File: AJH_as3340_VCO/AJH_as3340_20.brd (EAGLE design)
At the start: 27.9 x 110.5 mm, 99 parts, among them IC1 LM4040 5.0V, IC2 TL072D, IC3 TL072D, IC4 TL072D, IC5 CEM3340SOIC16, IC6 TL072D, IC7 TL072D

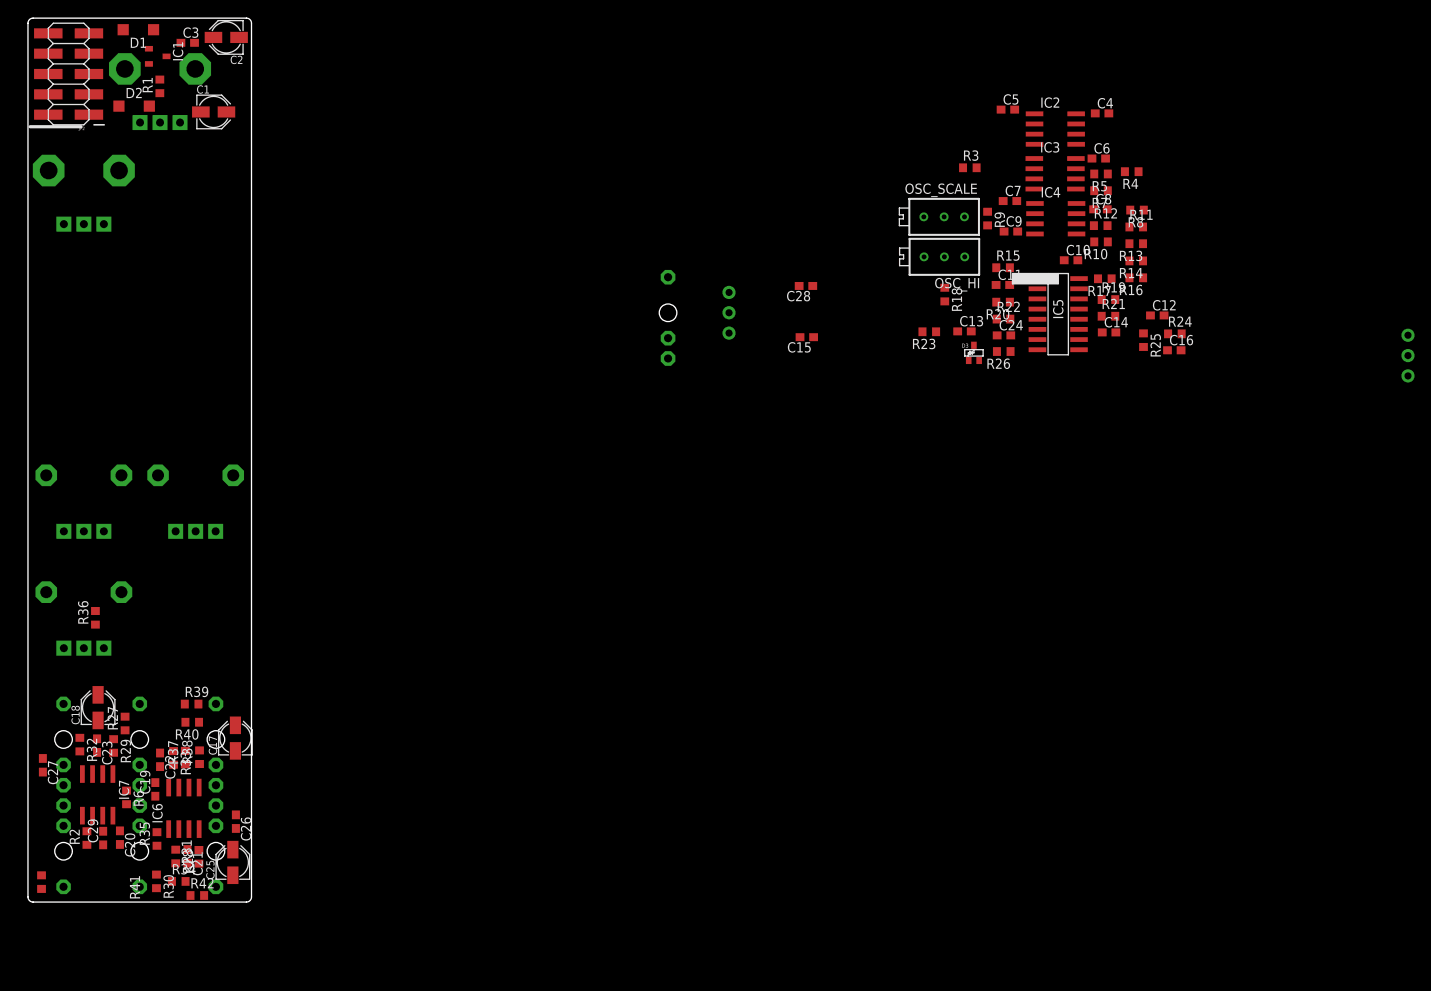
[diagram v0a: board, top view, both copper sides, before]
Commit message: Added Art Deco Panel template
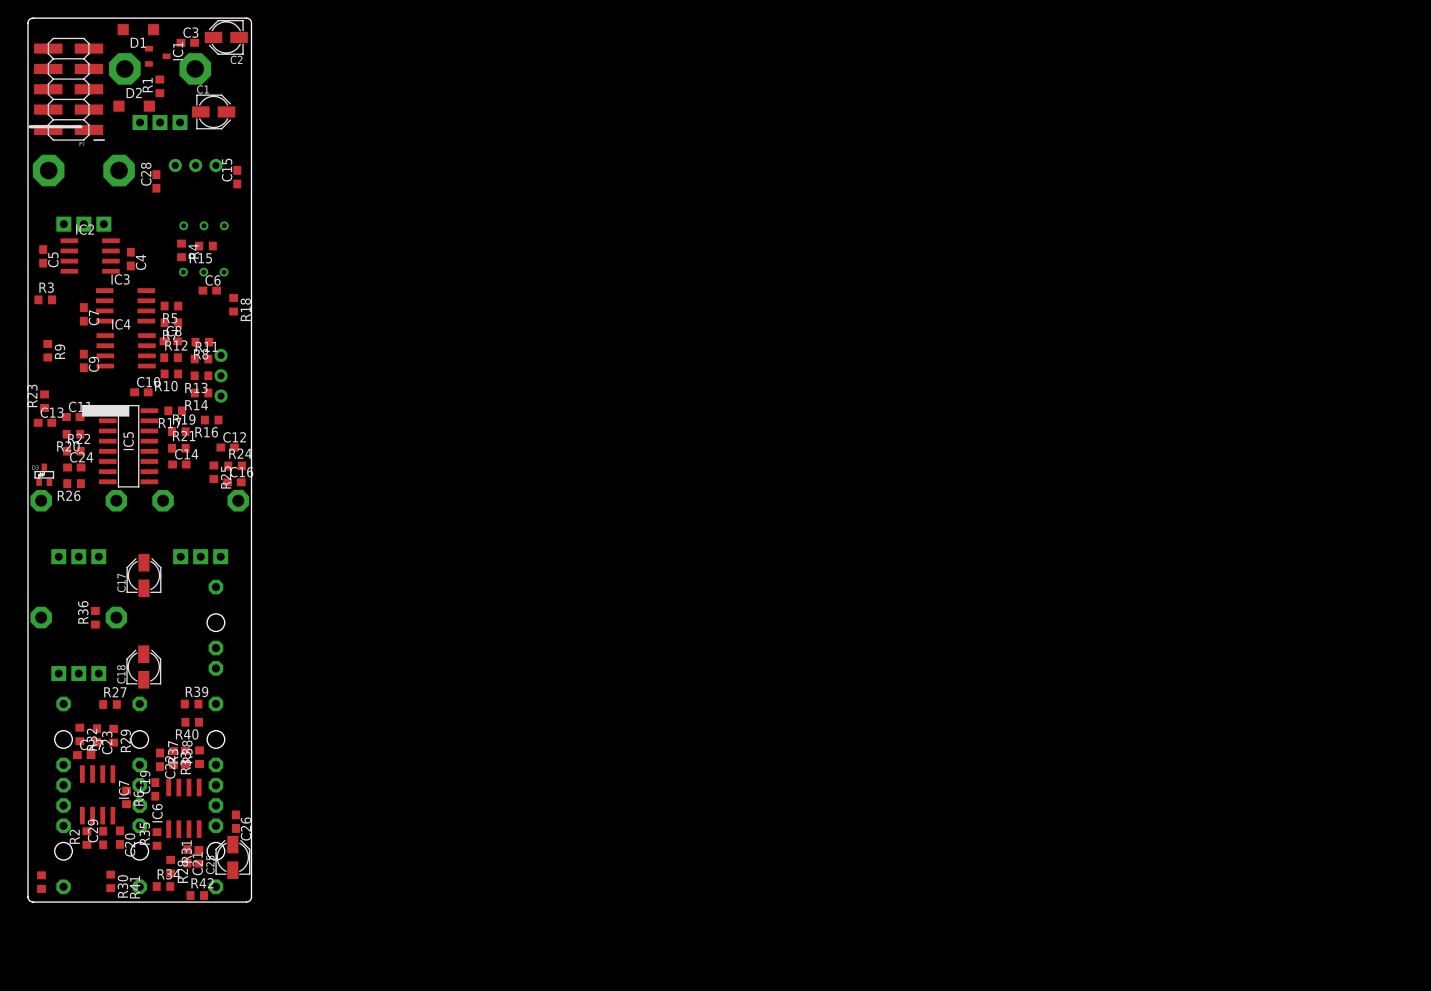
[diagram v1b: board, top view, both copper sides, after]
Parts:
- moved FM_SW 148.4 mm to (25.4, 74.7)
- moved C4 122.8 mm to (14.1, 89.3), turned to 270 degrees
- moved C5 122.0 mm to (3.17, 89.6), turned to 270 degrees
- moved IC2 121.7 mm to (9.04, 89.6)
- moved R4 119.2 mm to (20.5, 90.3), turned to 270 degrees
- moved R9 118.6 mm to (3.75, 77.8)
- moved C16 118.6 mm to (27.1, 61.4)
- moved R24 118.6 mm to (27.2, 63.4)
- moved R8 118.0 mm to (23.1, 78.9)
- moved R11 118.0 mm to (23.0, 76.8)
- moved R13 118.0 mm to (23.0, 74.7)
- moved R14 118.0 mm to (23.0, 72.5)
- moved C10 117.4 mm to (15.4, 72.6)
- moved C12 117.4 mm to (26.2, 65.7)
- moved C24 117.4 mm to (7.06, 63.2)
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
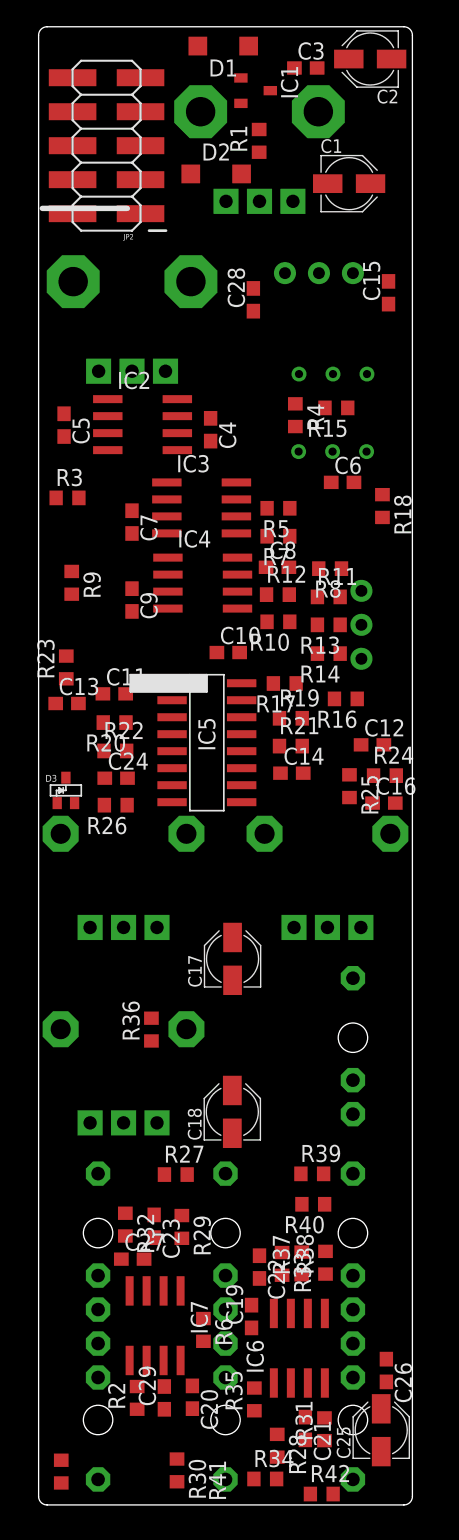
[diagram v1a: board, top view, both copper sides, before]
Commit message: Arranged parts to grid
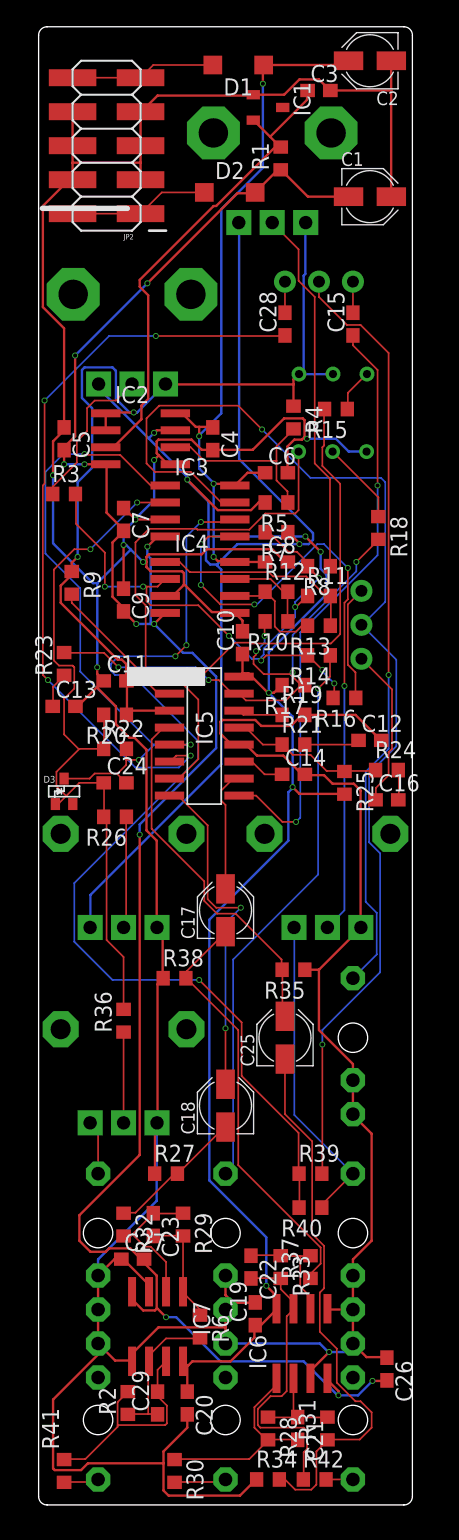
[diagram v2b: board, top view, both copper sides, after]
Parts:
- moved R35 32.2 mm to (20.3, 48.9), turned to 180 degrees
- moved C25 30.2 mm to (19.7, 43.8)
- moved R38 24.1 mm to (11.4, 48.3), turned to 0 degrees
- moved C6 4.99 mm to (19.1, 86.0)
- moved C17 3.67 mm to (15.2, 53.3)
- moved C15 3.55 mm to (24.8, 97.2)
- moved C28 2.98 mm to (19.7, 97.2)
- moved R36 2.19 mm to (7.62, 45.1)
- moved R1 2.08 mm to (19.4, 109.5)
- moved C3 1.95 mm to (22.2, 114.6)
- moved OSC_COARSE 1.85 mm to (18.7, 111.4)
- moved C1 1.83 mm to (26.0, 106.7)
- moved D1 1.80 mm to (16.2, 116.5)
- moved D2 1.72 mm to (15.6, 107.0)
- moved R18 1.67 mm to (26.7, 81.9)
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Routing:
- net GND: track 0.00 -> 364.8 mm, vias 0 -> 8
- net 12V: track 0.00 -> 151.8 mm, vias 0 -> 9
- net -12V: track 0.00 -> 149.4 mm, vias 0 -> 11
- net 5V: track 0.00 -> 93.4 mm, vias 0 -> 3
- net N$12: track 0.00 -> 88.3 mm, vias 0 -> 2
- net N$5: track 0.00 -> 77.3 mm, vias 0 -> 4
- net -5V: track 0.00 -> 72.4 mm, vias 0 -> 2
- net PWM_2_IN_SUM: track 0.00 -> 56.6 mm, vias 0 -> 2
- net N$94: track 0.00 -> 56.6 mm, vias 0 -> 4
- net SYNC_IN: track 0.00 -> 56.6 mm, vias 0 -> 1
- net PWM_IN: track 0.00 -> 48.4 mm, vias 0 -> 3
- net N$3: track 0.00 -> 47.5 mm, vias 0 -> 5
- net N$7: track 0.00 -> 46.6 mm, vias 0 -> 8
- net N$28: track 0.00 -> 44.7 mm, vias 0 -> 2
- net N$10: track 0.00 -> 42.0 mm, vias 0 -> 1
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
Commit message: Arranged UI
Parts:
- JP2: value M05X2SMD -> (none); device og-header:2X5-SMD -> jumper:JP5Q
- moved SYNC_SW 30.9 mm to (5.08, 74.6), turned to 0 degrees
- moved R35 12.5 mm to (9.21, 54.6), turned to 90 degrees
- moved IC2 12.4 mm to (7.94, 101.0)
- moved C5 10.1 mm to (7.94, 97.5), turned to 180 degrees
- moved R15 8.55 mm to (26.7, 82.9), turned to 270 degrees
- moved R9 8.36 mm to (10.8, 73.3), turned to 0 degrees
- moved R4 4.76 mm to (16.5, 93.0), turned to 180 degrees
- moved OSC_FINE 3.82 mm to (7.94, 95.6)
- moved C6 3.38 mm to (16.8, 88.6), turned to 90 degrees
- moved R18 3.01 mm to (23.8, 82.9)
- moved R24 2.86 mm to (27.3, 61.0)
- moved R3 2.84 mm to (4.45, 81.9), turned to 270 degrees
- moved OSC_COARSE 2.84 mm to (20.0, 108.9)
- moved D2 2.25 mm to (15.2, 104.8)
- moved C1 2.22 mm to (26.0, 104.5)
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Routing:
- net SOFTSYNC_IN: track 2.33 -> 41.3 mm, vias 0 -> 3
- net -12V: track 149.4 -> 174.4 mm, vias 11 -> 5
- net HARDSYNC_IN: track 2.33 -> 26.8 mm, vias 0 -> 3
- net N$31: track 31.6 -> 53.5 mm, vias 0 -> 6
- net N$28: track 44.7 -> 62.8 mm, vias 2 -> 4
- net N$5: track 77.3 -> 59.5 mm, vias 4 -> 2
- net -5V: track 72.4 -> 88.9 mm, vias 2 -> 4
- net SYNC_IN: track 56.6 -> 40.2 mm, vias 1 -> 4
- net PULSE_OUT: track 27.4 -> 43.0 mm, vias 0 -> 2
- net N$10: track 42.0 -> 56.7 mm, vias 1 -> 2
- net GND: track 364.8 -> 379.4 mm, vias 8 -> 9
- net PWM_IN: track 48.4 -> 34.0 mm, vias 3 -> 4
- net 12V: track 151.8 -> 163.9 mm, vias 9 -> 11
- net N$12: track 88.3 -> 77.1 mm
- net -5VIN: track 36.8 -> 26.5 mm, vias 0 -> 2
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- added copper zone on layer 1, net GND
- added copper zone on layer 16, net GND

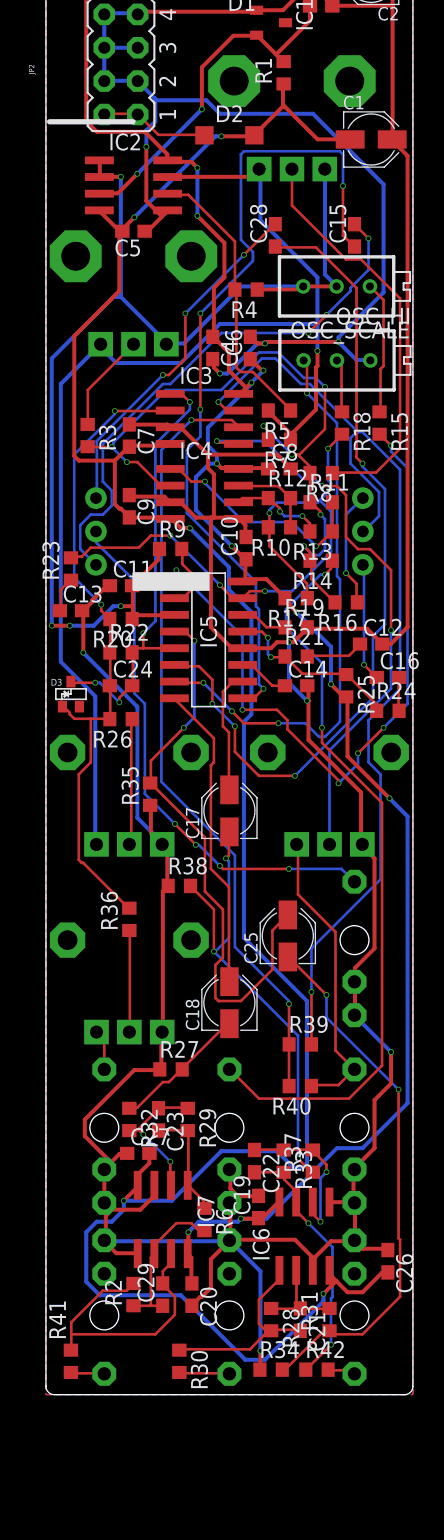
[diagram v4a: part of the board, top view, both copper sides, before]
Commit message: Mirrored holes to FP
UI DESIGN FREEZE!!
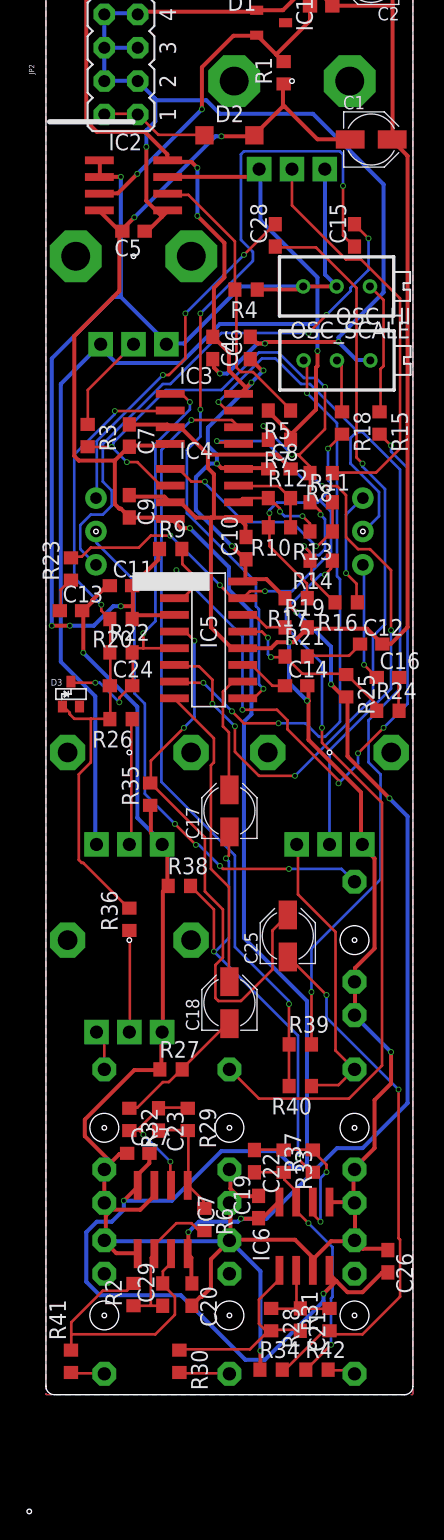
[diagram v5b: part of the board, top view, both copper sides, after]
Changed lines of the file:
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@@
 <drawing>
 <settings>
-<setting alwaysvectorfont="no"/>
+<setting alwaysvectorfont="yes"/>
 <setting verticaltext="up"/>
 </settings>
@@
 <layer number="17" name="Pads" color="2" fill="1" visible="no" active="yes"/>
 <layer number="18" name="Vias" color="2" fill="1" visible="no" active="yes"/>
-<layer number="19" name="Unrouted" color="6" fill="1" visible="yes" active="yes"/>
+<layer number="19" name="Unrouted" color="6" fill="1" visible="no" active="yes"/>
 <layer number="20" name="Dimension" color="24" fill="1" visible="yes" active="yes"/>
 <layer number="21" name="tPlace" color="7" fill="1" visible="no" active="yes"/>
@@
 <layer number="38" name="bTest" color="7" fill="1" visible="no" active="yes"/>
 <layer number="39" name="tKeepout" color="4" fill="11" visible="no" active="yes"/>
-<layer number="40" name="bKeepout" color="1" fill="11" visible="yes" active="yes"/>
+<layer number="40" name="bKeepout" color="1" fill="11" visible="no" active="yes"/>
 <layer number="41" name="tRestrict" color="4" fill="10" visible="no" active="yes"/>
-<layer number="42" name="bRestrict" color="1" fill="10" visible="yes" active="yes"/>
+<layer number="42" name="bRestrict" color="1" fill="10" visible="no" active="yes"/>
 <layer number="43" name="vRestrict" color="2" fill="10" visible="no" active="yes"/>
 <layer number="44" name="Drills" color="7" fill="1" visible="no" active="yes"/>
-<layer number="45" name="Holes" color="7" fill="1" visible="no" active="yes"/>
+<layer number="45" name="Holes" color="7" fill="1" visible="yes" active="yes"/>
 <layer number="46" name="Milling" color="3" fill="1" visible="no" active="yes"/>
 <layer number="47" name="Measures" color="7" fill="1" visible="no" active="yes"/>
@@
 <wire x1="1.5494" y1="105.8037" x2="7.8994" y2="105.8037" width="0.4064" layer="21"/>
 <circle x="0" y="0" radius="2.2450625" width="0.1524" layer="22"/>
+<hole x="20.0025" y="108.9025" drill="0.35"/>
+<hole x="7.9375" y="95.5675" drill="0.35"/>
+<hole x="25.4" y="74.6125" drill="0.35"/>
+<hole x="5.08" y="74.6125" drill="0.35"/>
+<hole x="22.86" y="57.785" drill="0.35"/>
+<hole x="7.62" y="57.785" drill="0.35"/>
+<hole x="24.765" y="43.4975" drill="0.35"/>
+<hole x="7.62" y="43.4975" drill="0.35"/>
+<hole x="15.24" y="29.21" drill="0.35"/>
+<hole x="24.765" y="29.21" drill="0.35"/>
+<hole x="5.715" y="29.21" drill="0.35"/>
+<hole x="24.765" y="14.9225" drill="0.35"/>
+<hole x="15.24" y="14.9225" drill="0.35"/>
+<hole x="5.715" y="14.9225" drill="0.35"/>
+<hole x="0" y="0" drill="0.35"/>
 </plain>
 <attributes>

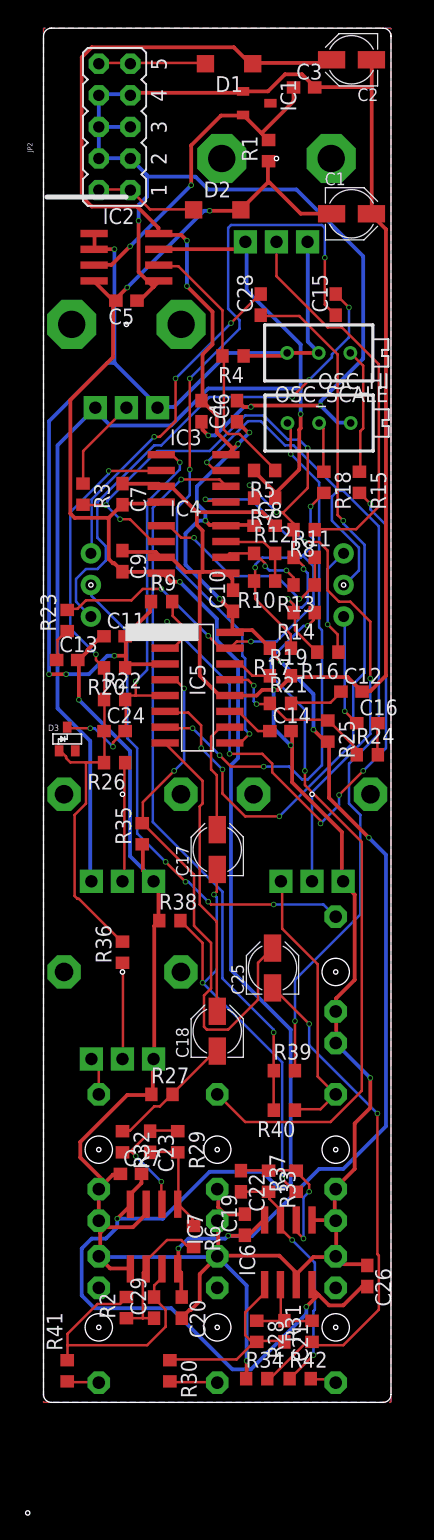
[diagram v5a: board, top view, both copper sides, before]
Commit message: Routing Done
Routed the PCB, no components modification is allowed!
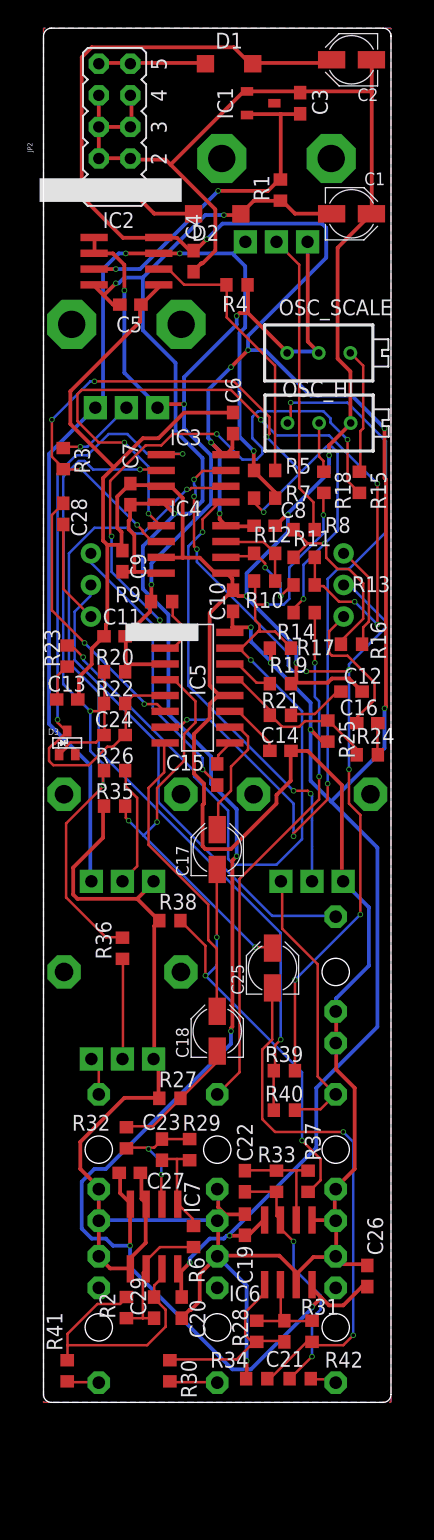
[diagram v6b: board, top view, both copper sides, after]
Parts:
- moved C15 39.0 mm to (15.2, 59.4), turned to 270 degrees
- moved C28 23.1 mm to (2.86, 80.3), turned to 270 degrees
- moved C4 12.1 mm to (13.3, 100.6)
- moved R4 5.72 mm to (16.8, 98.7)
- moved R1 3.31 mm to (20.3, 106.4)
- moved R3 3.27 mm to (2.86, 84.8)
- moved C13 3.17 mm to (3.17, 65.4)
- moved R35 3.14 mm to (6.99, 56.8), turned to 0 degrees
- moved R23 2.86 mm to (3.17, 68.9)
- moved R16 2.01 mm to (26.0, 69.8)
- moved C14 1.59 mm to (20.3, 61.3)
- moved C3 1.31 mm to (21.9, 113.3), turned to 90 degrees
- moved C23 1.14 mm to (10.8, 29.2)
- moved R29 1.14 mm to (13.0, 29.2)
- moved C6 1.00 mm to (16.5, 87.6)
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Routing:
- net N$28: track 62.8 -> 2.14 mm, vias 4 -> 0
- net 12V: track 163.9 -> 210.4 mm, vias 11 -> 12
- net N$8: track 17.6 -> 61.9 mm, vias 2 -> 6
- net N$94: track 63.3 -> 21.5 mm, vias 4 -> 2
- net N$7: track 54.2 -> 79.8 mm, vias 7 -> 8
- net PITCH_IN: track 46.3 -> 70.8 mm, vias 5 -> 4
- net N$100: track 43.5 -> 62.1 mm
- net HARDSYNC_IN: track 26.8 -> 8.33 mm, vias 3 -> 0
- net SOFTSYNC_IN: track 41.3 -> 22.9 mm, vias 3 -> 1
- net PWM_IN: track 34.0 -> 51.3 mm, vias 4 -> 2
- net N$10: track 56.7 -> 42.3 mm
- net -5V: track 88.9 -> 76.1 mm
- net PWM_2_IN_SUM: track 50.7 -> 62.8 mm, vias 2 -> 3
- net PULSE_OUT: track 43.0 -> 32.8 mm, vias 2 -> 3
- net N$5: track 59.5 -> 67.3 mm
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- added copper zone on layer 16, net N$41
- removed copper zone on layer 16, net GND
